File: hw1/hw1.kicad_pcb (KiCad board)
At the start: 2 copper layers, 53.9 x 53.3 mm, 35 parts, among them J1 CONN_01X02, J10 TEST_1P, J11 TEST_1P, J2 TEST_1P, J3 TEST_1P, J4 TEST_1P, J5 TEST_1P, J7 TEST_1P, J8 TEST_1P, J9 TEST_1P, P1 Power, P10 CONTROL, P11 CONN_01X06, P2 Analog, P3 Digital, P4 Digital, P9 FX2LA, U1 STM32L151C6TxA, U2 MIC550x-3.3YM5, Y1 Crystal_GND24_Small

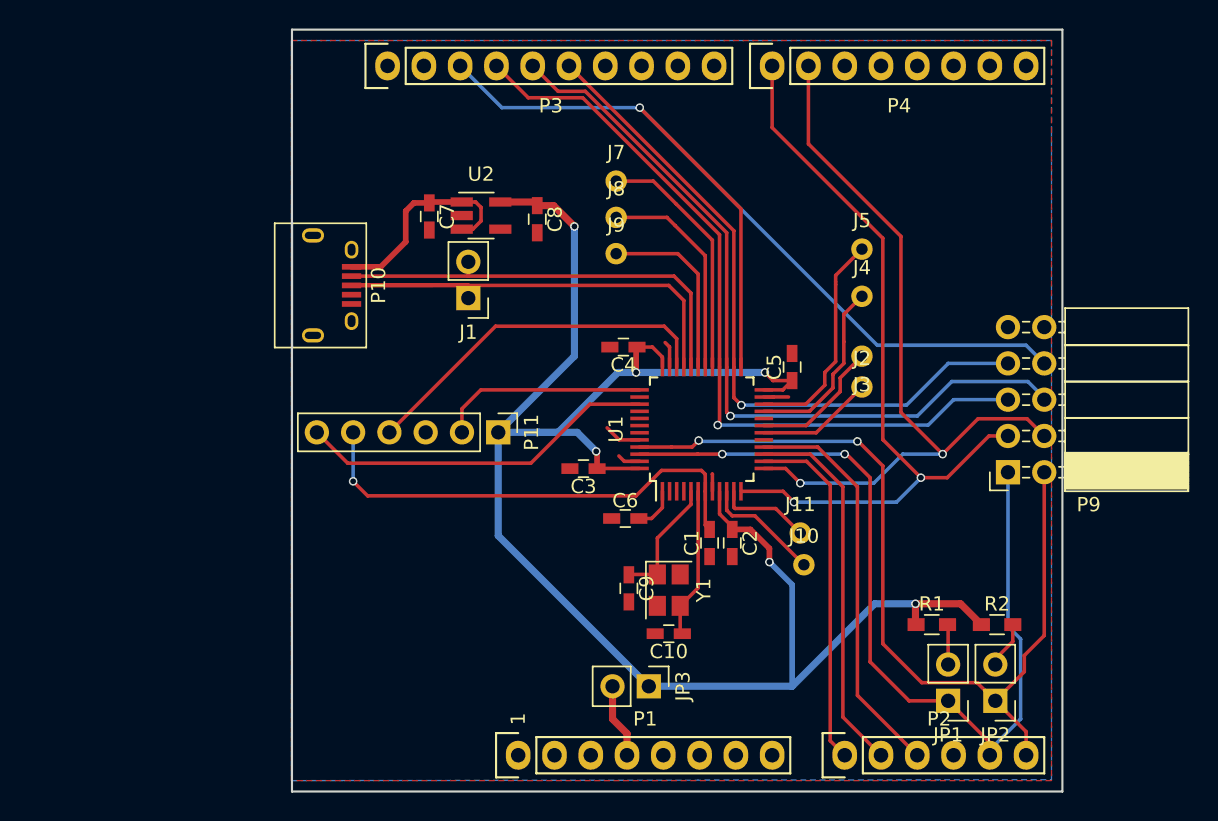
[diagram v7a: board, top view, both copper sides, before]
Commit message: hw1: cleanup silk and start adding labels
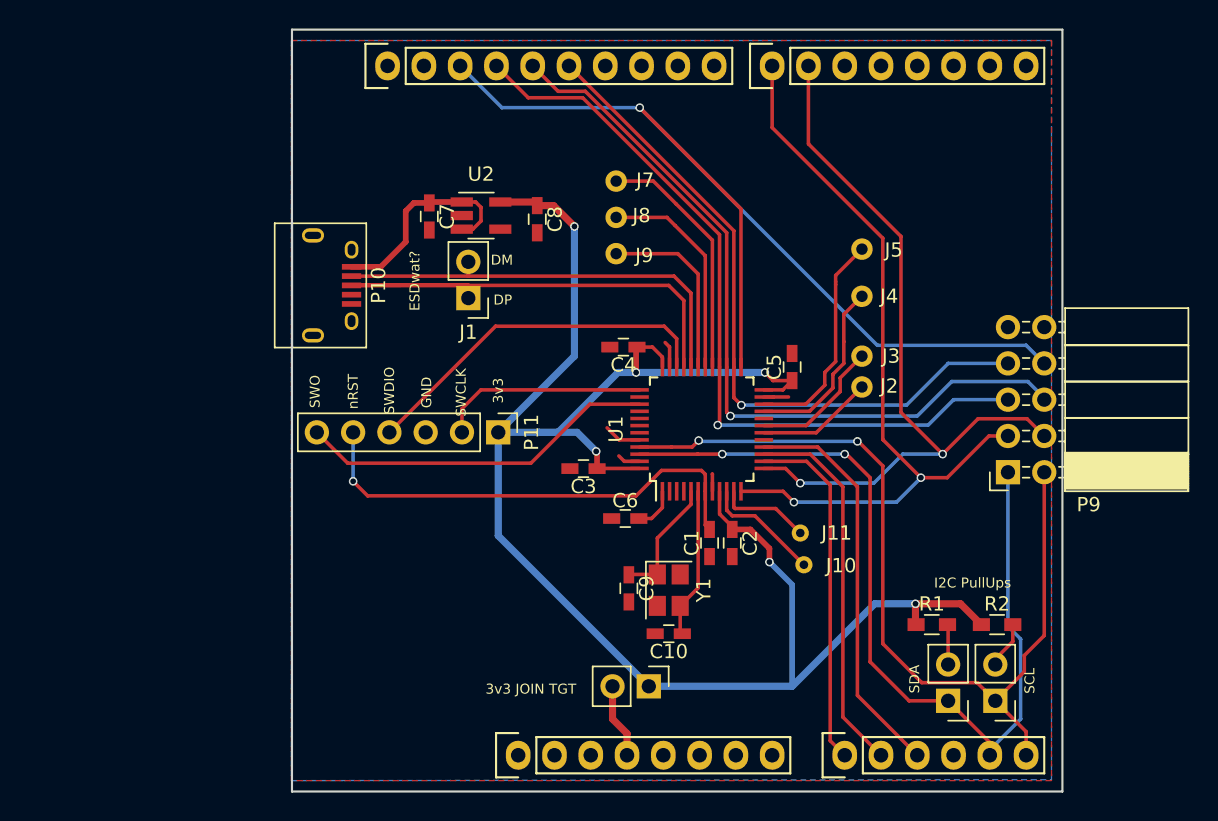
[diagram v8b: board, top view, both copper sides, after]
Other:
- board text added: "3v3"
- board text added: "3v3 JOIN TGT"
- board text added: "DM"
- board text added: "DP"
- board text added: "ESDwat?"
- board text added: "GND"
- board text added: "I2C PullUps"
- board text added: "SCL"
- board text added: "SDA"
- board text added: "SWCLK"
- board text added: "SWDIO"
- board text added: "SWO"
- board text added: "nRST"
- board text removed: "1"
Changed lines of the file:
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@@
     (links 87)
     (no_connects 24)
-    (area 104.572999 72.949999 186.303001 126.440001)
+    (area 119.9355 72.949999 186.303001 126.440001)
     (thickness 1.6)
-    (drawings 5)
+    (drawings 17)
     (tracks 288)
     (zones 0)
@@
   )
   (setup
-    (last_trace_width 0.5)
+    (last_trace_width 0.25)
     (user_trace_width 0.152)
     (user_trace_width 0.25)
@@
     (mod_text_width 0.15)
     (pad_size 1.2 1.2)
-    (pad_drill 0.8001)
+    (pad_drill 0.6)
     (pad_to_mask_clearance 0)
     (aux_axis_origin 123.1265 126.365)
     (grid_origin 110.998 126.365)
-    (visible_elements FFFEFF7F)
+    (visible_elements FFFEFFFF)
     (pcbplotparams
-      (layerselection 0x00030_80000001)
+      (layerselection 0x00020_00000000)
       (usegerberextensions false)
       (excludeedgelayer true)
@@
       (outputformat 1)
       (mirror false)
-      (drillshape 1)
+      (drillshape 0)
       (scaleselection 1)
       (outputdirectory ""))
@@
     (descr "Through hole socket strip")
     (tags "socket strip")
-    (fp_text reference P1 (at 8.89 -2.54) (layer F.SilkS)
+    (fp_text reference P1 (at 8.89 -2.54) (layer F.SilkS) hide
       (effects (font (size 1 1) (thickness 0.15)))
     )
@@
     (descr "Through hole socket strip")
     (tags "socket strip")
-    (fp_text reference P2 (at 6.604 -2.54) (layer F.SilkS)
+    (fp_text reference P2 (at 6.604 -2.54) (layer F.SilkS) hide
       (effects (font (size 1 1) (thickness 0.15)))
     )
@@
     (descr "Through hole socket strip")
     (tags "socket strip")
-    (fp_text reference P3 (at 11.43 2.794) (layer F.SilkS)
+    (fp_text reference P3 (at 11.43 2.794) (layer F.SilkS) hide
       (effects (font (size 1 1) (thickness 0.15)))
     )
@@
     (descr "Through hole socket strip")
     (tags "socket strip")
-    (fp_text reference P4 (at 8.89 2.794) (layer F.SilkS)
+    (fp_text reference P4 (at 8.89 2.794) (layer F.SilkS) hide
       (effects (font (size 1 1) (thickness 0.15)))
     )
@@
     (tags "Mesurement Point Round Trough Hole 1.5mm Drill 0.8mm")
     (attr virtual)
-    (fp_text reference J2 (at 0 -2) (layer F.SilkS)
+    (fp_text reference J2 (at 1.905 -0.0635) (layer F.SilkS)
       (effects (font (size 1 1) (thickness 0.15)))
     )
@@
     (tags "Mesurement Point Round Trough Hole 1.5mm Drill 0.8mm")
     (attr virtual)
-    (fp_text reference J4 (at 0 -2) (layer F.SilkS)
+    (fp_text reference J4 (at 1.905 0) (layer F.SilkS)
       (effects (font (size 1 1) (thickness 0.15)))
     )
@@
     (tags "Mesurement Point Round Trough Hole 1.5mm Drill 0.8mm")
     (attr virtual)
-    (fp_text reference J7 (at 0 -2) (layer F.SilkS)
+    (fp_text reference J7 (at 2.032 -0.0635) (layer F.SilkS)
       (effects (font (size 1 1) (thickness 0.15)))
     )
@@
     (tags "Mesurement Point Round Trough Hole 1.5mm Drill 0.8mm")
     (attr virtual)
-    (fp_text reference J5 (at 0 -2) (layer F.SilkS)
+    (fp_text reference J5 (at 2.2225 0.0635) (layer F.SilkS)
       (effects (font (size 1 1) (thickness 0.15)))
     )
@@
     (tags "Mesurement Point Round Trough Hole 1.5mm Drill 0.8mm")
     (attr virtual)
-    (fp_text reference J8 (at 0 -2) (layer F.SilkS)
+    (fp_text reference J8 (at 1.778 -0.127) (layer F.SilkS)
       (effects (font (size 1 1) (thickness 0.15)))
     )
@@
     (tags "Mesurement Point Round Trough Hole 1.5mm Drill 0.8mm")
     (attr virtual)
-    (fp_text reference J9 (at 0 -2) (layer F.SilkS)
+    (fp_text reference J9 (at 1.9685 0.127) (layer F.SilkS)
       (effects (font (size 1 1) (thickness 0.15)))
     )
@@
     (tags "Mesurement Point Round Trough Hole 1.5mm Drill 0.8mm")
     (attr virtual)
-    (fp_text reference J3 (at 0 -2 180) (layer F.SilkS)
+    (fp_text reference J3 (at -2.032 0 180) (layer F.SilkS)
       (effects (font (size 1 1) (thickness 0.15)))
     )
@@
     (tags "Mesurement Point Round Trough Hole 1.5mm Drill 0.8mm")
     (attr virtual)
-    (fp_text reference J10 (at 0 -2) (layer F.SilkS)
+    (fp_text reference J10 (at 2.6035 0.0635) (layer F.SilkS)
       (effects (font (size 1 1) (thickness 0.15)))
     )
@@
     )
     (fp_circle (center 0 0) (end 1 0) (layer F.CrtYd) (width 0.05))
-    (pad 1 thru_hole circle (at 0 0) (size 1.5 1.5) (drill 0.8) (layers *.Cu *.Mask)
+    (pad 1 thru_hole circle (at 0 0) (size 1.2 1.2) (drill 0.6) (layers *.Cu *.Mask)
       (net 35 "Net-(J10-Pad1)"))
   )
@@
     (tags "Mesurement Point Round Trough Hole 1.5mm Drill 0.8mm")
     (attr virtual)
-    (fp_text reference J11 (at 0 -2) (layer F.SilkS)
+    (fp_text reference J11 (at 2.54 0) (layer F.SilkS)
       (effects (font (size 1 1) (thickness 0.15)))
     )
@@
     )
     (fp_circle (center 0 0) (end 1 0) (layer F.CrtYd) (width 0.05))
-    (pad 1 thru_hole circle (at 0 0) (size 1.5 1.5) (drill 0.8) (layers *.Cu *.Mask)
+    (pad 1 thru_hole circle (at 0 0) (size 1.2 1.2) (drill 0.6) (layers *.Cu *.Mask)
       (net 36 "Net-(J11-Pad1)"))
   )
@@
     (descr "Through hole straight pin header, 1x02, 2.54mm pitch, single row")
     (tags "Through hole pin header THT 1x02 2.54mm single row")
-    (fp_text reference JP1 (at 0 -2.39 180) (layer F.SilkS)
+    (fp_text reference JP1 (at 0 -2.39 180) (layer F.SilkS) hide
       (effects (font (size 1 1) (thickness 0.15)))
     )
@@
     (descr "Through hole straight pin header, 1x02, 2.54mm pitch, single row")
     (tags "Through hole pin header THT 1x02 2.54mm single row")
-    (fp_text reference JP2 (at 0 -2.39 180) (layer F.SilkS)
+    (fp_text reference JP2 (at 0 -2.39 180) (layer F.SilkS) hide
       (effects (font (size 1 1) (thickness 0.15)))
     )
@@
     (descr "Through hole straight pin header, 1x02, 2.54mm pitch, single row")
     (tags "Through hole pin header THT 1x02 2.54mm single row")
-    (fp_text reference JP3 (at 0 -2.39 270) (layer F.SilkS)
+    (fp_text reference JP3 (at 0 -2.39 270) (layer F.SilkS) hide
       (effects (font (size 1 1) (thickness 0.15)))
     )
@@
     )
   )
-  (gr_text 1 (at 138.938 121.285 90) (layer F.SilkS)
-    (effects (font (size 1 1) (thickness 0.15)))
+  (gr_text 3v3 (at 137.541 98.298 90) (layer F.SilkS)
+    (effects (font (size 0.7 0.7) (thickness 0.12)))
+  )
+  (gr_text SWCLK (at 134.9375 98.425 90) (layer F.SilkS)
+    (effects (font (size 0.7 0.7) (thickness 0.12)))
+  )
+  (gr_text GND (at 132.5245 98.425 90) (layer F.SilkS)
+    (effects (font (size 0.7 0.7) (thickness 0.12)))
+  )
+  (gr_text SWDIO (at 129.921 98.298 90) (layer F.SilkS)
+    (effects (font (size 0.7 0.7) (thickness 0.12)))
+  )
+  (gr_text nRST (at 127.381 98.3615 90) (layer F.SilkS)
+    (effects (font (size 0.7 0.7) (thickness 0.12)))
+  )
+  (gr_text SWO (at 124.714 98.3615 90) (layer F.SilkS)
+    (effects (font (size 0.7 0.7) (thickness 0.12)))
+  )
+  (gr_text "I2C PullUps" (at 170.7515 111.76) (layer F.SilkS)
+    (effects (font (size 0.7 0.7) (thickness 0.175)))
+  )
+  (gr_text SCL (at 174.752 118.618 90) (layer F.SilkS)
+    (effects (font (size 0.7 0.7) (thickness 0.175)))
+  )
+  (gr_text SDA (at 166.6875 118.491 90) (layer F.SilkS)
+    (effects (font (size 0.7 0.7) (thickness 0.175)))
+  )
+  (gr_text "3v3 JOIN TGT" (at 139.827 119.1895) (layer F.SilkS)
+    (effects (font (size 0.7 0.7) (thickness 0.175)))
+  )
+  (gr_text DP (at 137.8585 91.948) (layer F.SilkS)
+    (effects (font (size 0.7 0.7) (thickness 0.12)))
+  )
+  (gr_text DM (at 137.795 89.154) (layer F.SilkS)
+    (effects (font (size 0.7 0.7) (thickness 0.12)))
+  )
+  (gr_text ESDwat? (at 131.699 90.6145 90) (layer F.SilkS)
+    (effects (font (size 0.7 0.7) (thickness 0.12)))
   )
   (gr_line (start 177.038 126.365) (end 177.038 73.025) (angle 90) (layer Edge.Cuts) (width 0.15))
